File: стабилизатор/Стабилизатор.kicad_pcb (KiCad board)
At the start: 2 copper layers, 35 parts, among them J1 V_IN, J2 +43V, J3 -43V, J4 +11V, J5 -11V, J6 +31V, J7 -31V, J8 V_OUT, Q1 BD140, Q2 BD139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

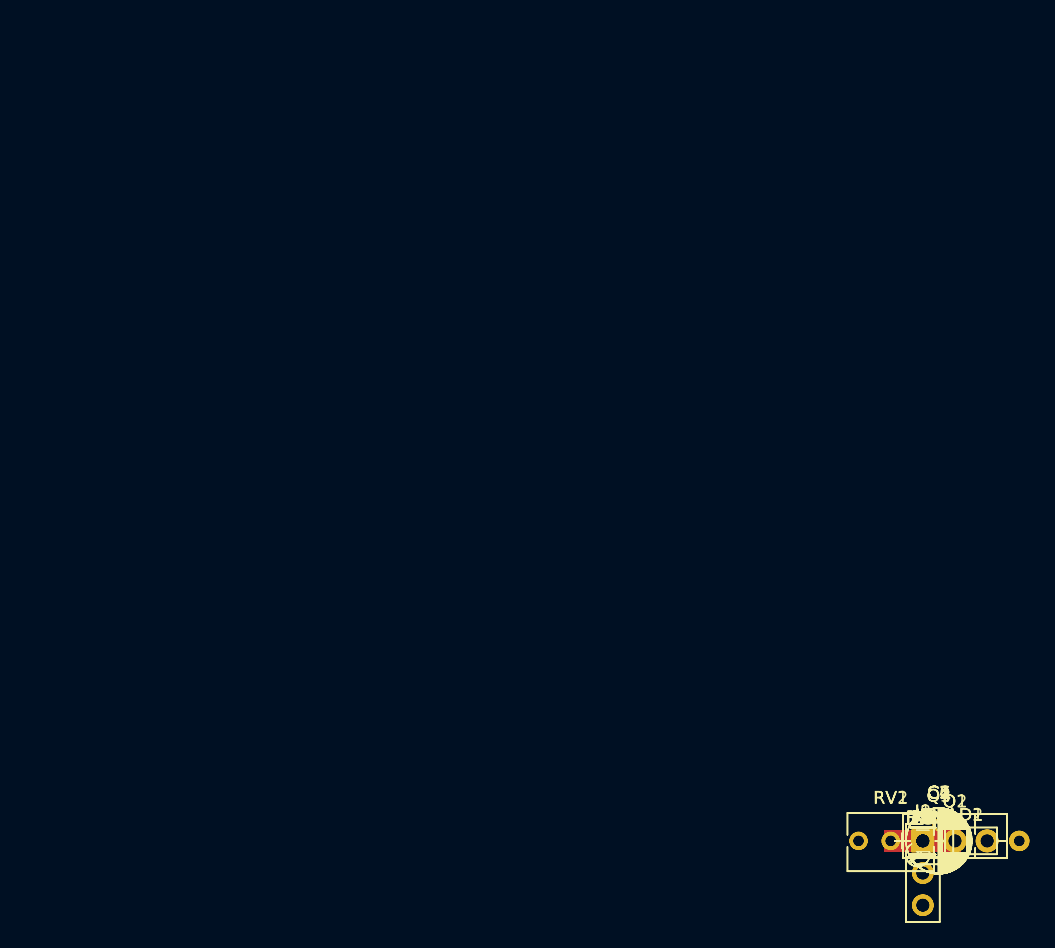
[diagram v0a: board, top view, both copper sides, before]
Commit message: Разводка платы стабилизатора
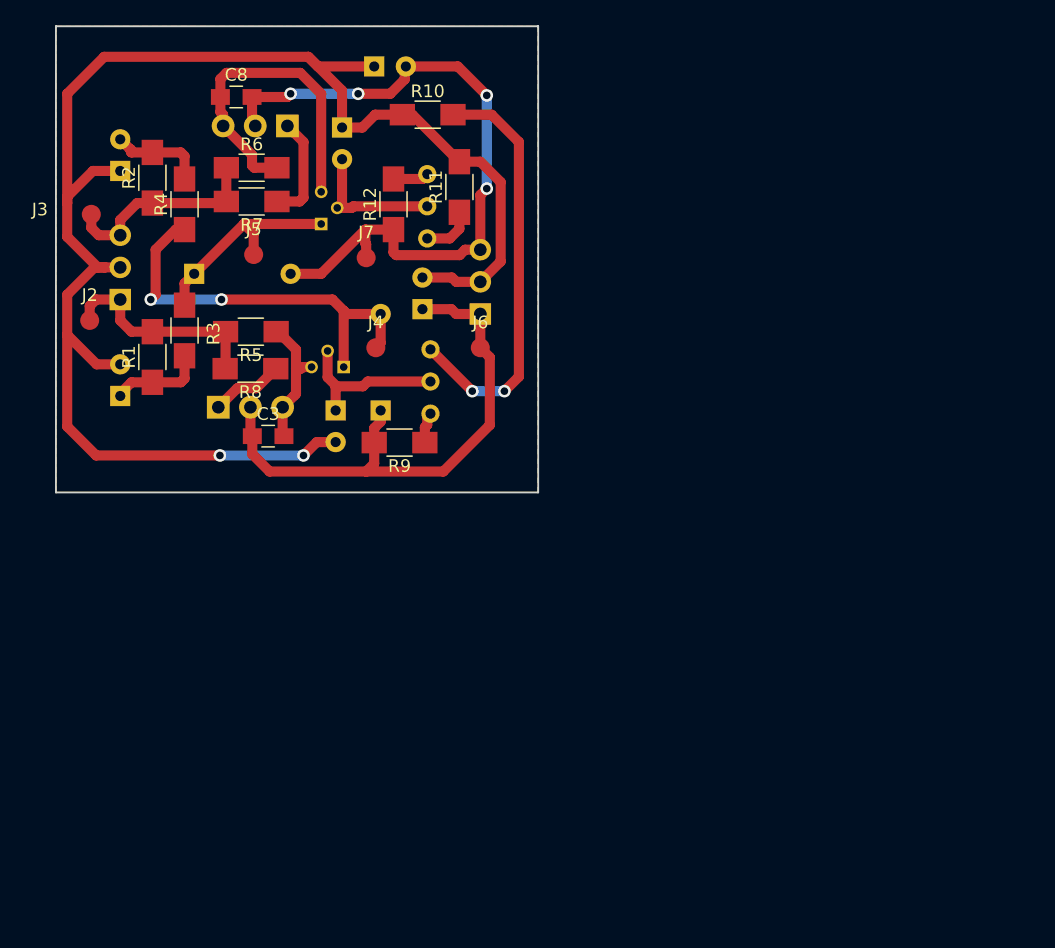
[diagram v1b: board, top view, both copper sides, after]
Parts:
- added C8: 120nF, Capacitors_SMD:C_0805_HandSoldering, F.Cu at (94.3, 46.2)
- C1, C2, C4, C5, C6, C7, D1, D2, J1, J8, Q1, Q2, Q3, Q4, RV1, RV2: moved to B.Cu
- moved C2 82.6 mm to (85.1, 52.1), turned to 90 degrees
- moved J3 82.3 mm to (82.8, 55.5)
- moved R2 80.3 mm to (87.6, 52.6), turned to 90 degrees
- moved J2 77.6 mm to (82.7, 63.9)
- moved R4 77.0 mm to (90.2, 54.7), turned to 90 degrees
- moved J1 76.5 mm to (85.1, 62.2)
- moved Q2 75.6 mm to (98.3, 48.5), turned to 180 degrees
- moved R6 75.1 mm to (95.5, 51.8)
- moved C7 75.0 mm to (105.2, 43.8)
- moved R7 73.2 mm to (95.5, 54.5), turned to 180 degrees
- moved D1 73.0 mm to (90.9, 60.2)
- moved C5 72.7 mm to (102.6, 48.6), turned to 270 degrees
- moved C1 72.5 mm to (85.1, 69.8), turned to 90 degrees
- moved R1 71.9 mm to (87.6, 66.8), turned to 90 degrees
- moved R3 70.9 mm to (90.2, 64.7), turned to 270 degrees
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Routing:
- net Net-(C1-Pad2): track 0.00 -> 125.0 mm, vias 0 -> 2
- net Net-(C7-Pad2): track 0.00 -> 56.6 mm, vias 0 -> 4
- net Net-(C3-Pad1): track 0.00 -> 43.7 mm
- net Net-(R10-Pad2): track 0.00 -> 33.5 mm, vias 0 -> 2
- net Net-(D2-Pad2): track 0.00 -> 32.6 mm, vias 0 -> 2
- net Net-(C8-Pad1): track 0.00 -> 26.5 mm
- net Net-(D1-Pad1): track 0.00 -> 17.2 mm
- net Net-(J1-Pad1): track 0.00 -> 17.0 mm
- net Net-(J1-Pad3): track 0.00 -> 16.4 mm
- net Net-(C4-Pad1): track 0.00 -> 12.6 mm
- net Net-(C5-Pad2): track 0.00 -> 11.2 mm
- net Net-(C3-Pad2): track 0.00 -> 10.8 mm
- net Net-(Q2-Pad1): track 0.00 -> 8.42 mm
- net Net-(C1-Pad1): track 0.00 -> 7.64 mm
- net Net-(C2-Pad2): track 0.00 -> 7.54 mm
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- added copper zone on F.Cu, net Net-(C1-Pad2)
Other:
- board outline added: 38.1 x 36.8 mm
- net class Default: via_dia 0.6 -> 1; via_drill 0.4 -> 0.6
- rule trace_min: 0.2 -> 0.4
- rule via_min_drill: 0.3 -> 0.6
- rule via_min_size: 0.4 -> 1
